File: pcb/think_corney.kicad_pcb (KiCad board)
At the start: 2 copper layers, 130.3 x 86.5 mm, 112 parts

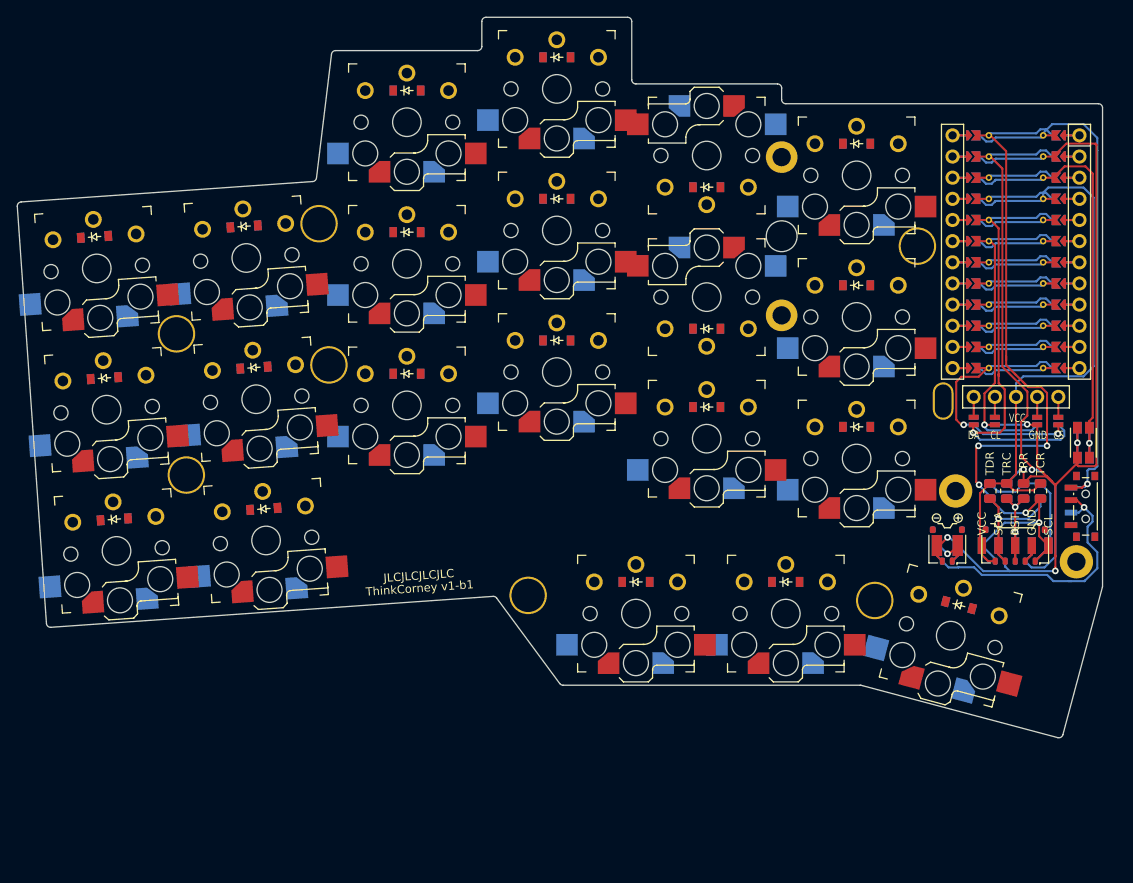
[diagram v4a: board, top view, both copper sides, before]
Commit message: Traces: Added initial matrix traces
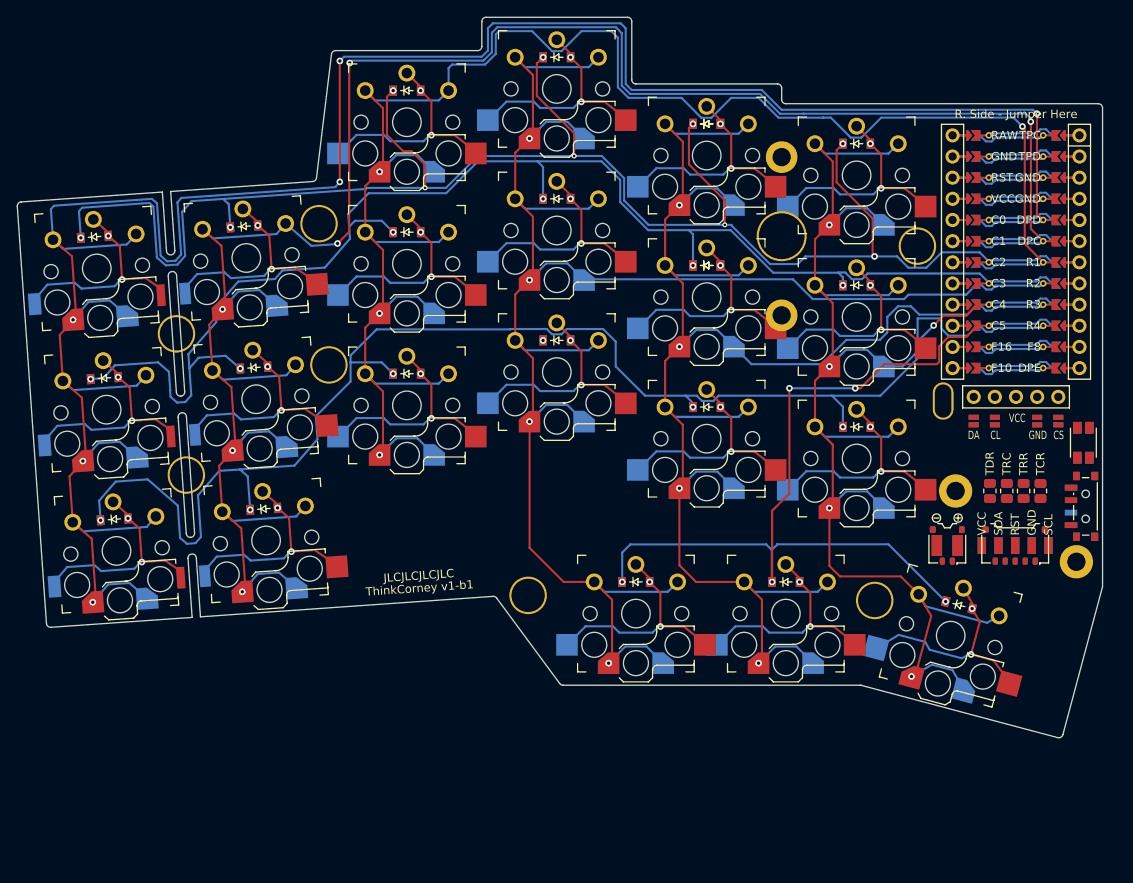
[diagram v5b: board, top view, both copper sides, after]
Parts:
- added D22: , ComboDiode, F.Cu at (170.9, 65.7)
- added D23: , ComboDiode, F.Cu at (170.9, 48.7)
- moved S19 96.0 mm to (115.6, 64.8), turned to -176 degrees
- moved S16 91.9 mm to (97.6, 66.1), turned to -176 degrees
- moved S15 90.7 mm to (98.8, 83.0), turned to -176 degrees
- moved S14 89.6 mm to (100.0, 100.0), turned to -176 degrees
- moved S12 68.7 mm to (180.4, 107.5)
- moved S18 68.6 mm to (116.8, 81.8), turned to -176 degrees
- moved S8 58.8 mm to (188.9, 88.9)
- moved S9 58.8 mm to (188.9, 71.9)
- moved D21 58.6 mm to (201.1, 106.5), turned to -15 degrees
- moved D18 53.3 mm to (188.9, 51.1)
- moved S11 47.0 mm to (162.4, 107.5)
- moved S17 45.3 mm to (118.0, 98.7), turned to -176 degrees
- moved D17 44.4 mm to (188.9, 68.1)
- moved S10 43.1 mm to (188.9, 54.9)
- moved S6 42.5 mm to (152.9, 44.5), turned to 180 degrees
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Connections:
- D14 pad 1: R3 -> R2
- D14 pad 2: inner_bottom -> index_home
- D15 pad 1: R2 -> R1
- D15 pad 2: inner_home -> index_top
- D16 pad 1: R1 -> R3
- D16 pad 2: inner_top -> inner_bottom
- D17 pad 1: R4 -> R2
- D17 pad 2: outer_cluster -> inner_home
- D18 pad 1: R4 -> R1
- D18 pad 2: home_cluster -> inner_top
- D19 pad 2: inner_cluster -> outer_cluster
- D20 pad 1: R2 -> R4
- D20 pad 2: index_home -> home_cluster
- D21 pad 1: R1 -> R4
- D21 pad 2: index_top -> inner_cluster
- MCU1 pad 113: F10 -> DPE
- MCU1 pad 114: F16 -> F8
- MCU1 pad 115: C5 -> R4
- MCU1 pad 116: C4 -> R3
- MCU1 pad 117: C3 -> R2
- MCU1 pad 118: C2 -> R1
- MCU1 pad 119: C1 -> DPC
- MCU1 pad 120: C0 -> DPD
- MCU1 pad 121: VCC -> GND
- MCU1 pad 122: RST -> GND
- MCU1 pad 123: GND -> TPD
- MCU1 pad 124: RAW -> TPC
- S1 pad 1: C0 -> C2
- S1 pad 2: outer_bottom -> ring_bottom
- S10 pad 1: C3 -> C5
- S10 pad 2: middle_bottom -> inner_top
- S11 pad 2: middle_home -> outer_cluster
- S12 pad 1: C3 -> C4
- S12 pad 2: middle_top -> home_cluster
- S13 pad 1: C4 -> C5
- S13 pad 2: index_bottom -> inner_cluster
- S14 pad 1: C5 -> C0
- S14 pad 2: inner_bottom -> outer_bottom
- S15 pad 1: C5 -> C0
- S15 pad 2: inner_home -> outer_home
- S16 pad 1: C5 -> C0
- S16 pad 2: inner_top -> outer_top
- S17 pad 1: C3 -> C1
- S17 pad 2: outer_cluster -> pinky_bottom
- S18 pad 1: C4 -> C1
- S18 pad 2: home_cluster -> pinky_home
- S19 pad 1: C5 -> C1
- S19 pad 2: inner_cluster -> pinky_top
- S2 pad 1: C0 -> C2
- S2 pad 2: outer_home -> ring_home
- S3 pad 1: C0 -> C2
- S3 pad 2: outer_top -> ring_top
- S4 pad 1: C1 -> C3
- S4 pad 2: pinky_bottom -> middle_bottom
- S5 pad 1: C1 -> C3
- S5 pad 2: pinky_home -> middle_home
- S6 pad 1: C1 -> C3
- S6 pad 2: pinky_top -> middle_top
- S7 pad 1: C2 -> C4
- S7 pad 2: ring_bottom -> index_bottom
- S8 pad 1: C2 -> C5
- S8 pad 2: ring_home -> inner_bottom
- S9 pad 1: C2 -> C5
- S9 pad 2: ring_top -> inner_home
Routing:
- net C0: track 10.1 -> 291.7 mm, vias 0 -> 6
- net C1: track 10.1 -> 254.1 mm, vias 0 -> 6
- net C2: track 10.1 -> 222.4 mm, vias 0 -> 4
- net C3: track 10.1 -> 219.3 mm, vias 0 -> 4
- net R1: track 10.2 -> 208.7 mm, vias 0 -> 10
- net C4: track 10.1 -> 206.3 mm, vias 0 -> 4
- net C5: track 10.1 -> 182.8 mm, vias 0 -> 4
- net R2: track 10.2 -> 173.4 mm, vias 0 -> 6
- net R3: track 10.2 -> 169.9 mm, vias 0 -> 7
- net GND: track 149.3 -> 30.5 mm, vias 5 -> 0
- net R4: track 10.2 -> 110.9 mm, vias 0 -> 5
- net VCC: track 96.3 -> 10.1 mm
- net F16: track 94.5 -> 10.1 mm, vias 5 -> 0
- net TPD: track 84.4 -> 10.2 mm, vias 2 -> 0
- net RAW: track 65.0 -> 10.1 mm, vias 1 -> 0
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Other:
- outline, holes or cut-outs redrawn

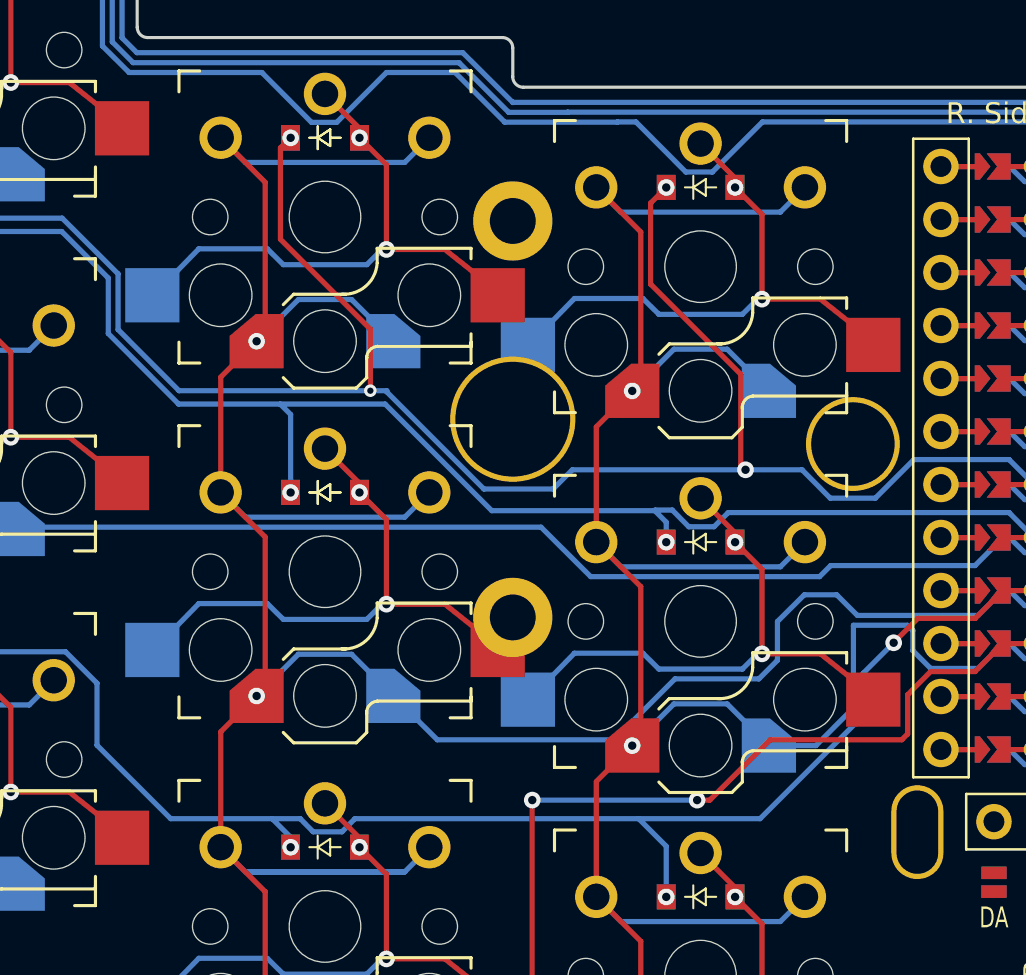
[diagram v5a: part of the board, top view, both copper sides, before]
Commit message: Traces: Fixed matrix traces for TP key changes
Added pcb
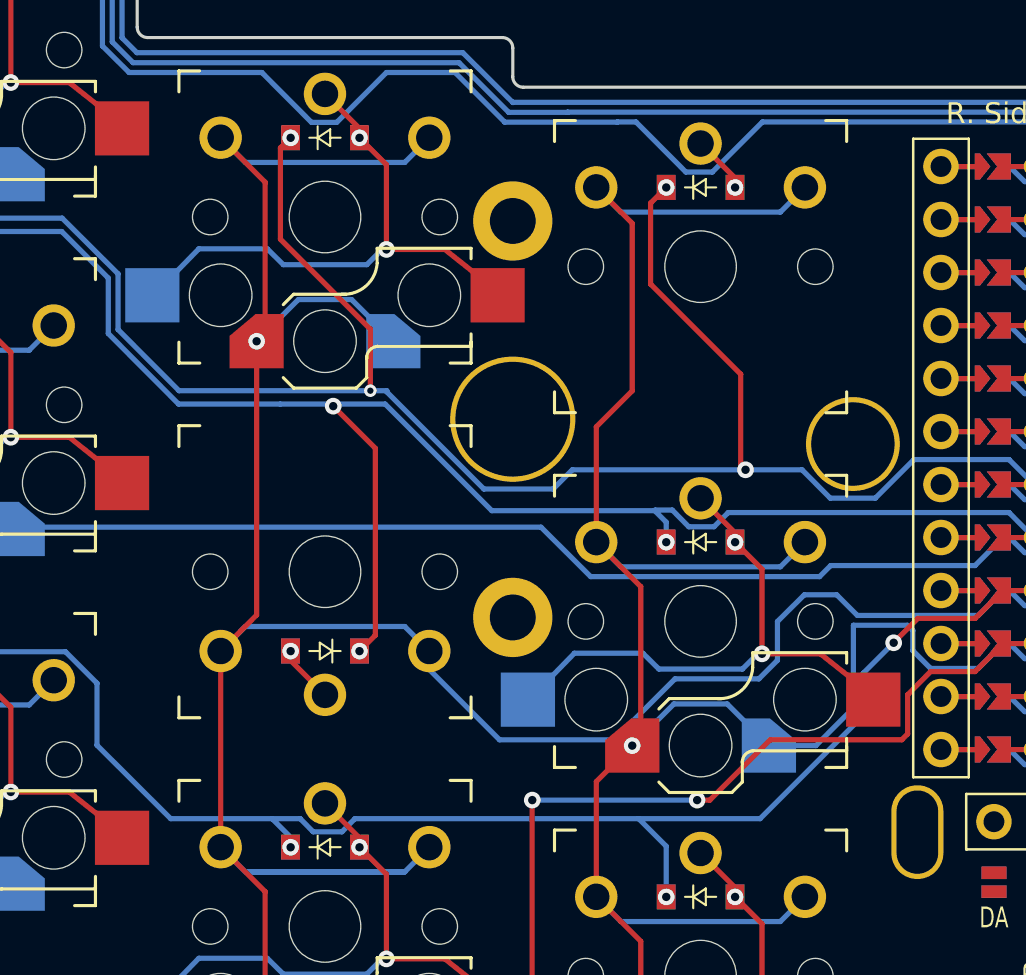
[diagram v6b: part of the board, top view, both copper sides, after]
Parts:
- removed D22, D23: , ComboDiode
- moved S13 104.9 mm to (98.8, 83.0), turned to -176 degrees
- moved S12 80.7 mm to (100.0, 100.0), turned to -176 degrees
- moved S18 61.5 mm to (170.9, 52.5), turned to 180 degrees
- moved D15 55.7 mm to (162.4, 103.7)
- moved S19 55.5 mm to (170.9, 69.5), turned to 180 degrees
- moved D20 53.3 mm to (188.9, 51.1)
- moved S10 53.3 mm to (180.4, 107.5)
- moved S9 44.4 mm to (162.4, 107.5)
- moved D17 40.3 mm to (201.1, 106.5), turned to -15 degrees
- moved D21 40.3 mm to (188.9, 68.1), turned to 0 degrees
- moved S11 37.9 mm to (200.2, 110.2), turned to 165 degrees
- moved S14 34.0 mm to (97.6, 66.1)
- moved S17 34.0 mm to (115.6, 64.8)
- moved D19 31.6 mm to (170.9, 73.3), turned to 180 degrees
- moved D14 26.4 mm to (188.9, 85.1)
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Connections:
- D14 pad 1: R2 -> R3
- D14 pad 2: index_home -> inner_bottom
- D15 pad 1: R1 -> R4
- D15 pad 2: index_top -> outer_cluster
- D16 pad 1: R3 -> R4
- D16 pad 2: inner_bottom -> home_cluster
- D17 pad 1: R2 -> R4
- D17 pad 2: inner_home -> inner_cluster
- D18 pad 2: inner_top -> index_top
- D19 pad 1: R4 -> R2
- D19 pad 2: outer_cluster -> index_home
- D20 pad 1: R4 -> R1
- D20 pad 2: home_cluster -> inner_top
- D21 pad 1: R4 -> R2
- D21 pad 2: inner_cluster -> inner_home
- S10 pad 1: C5 -> C4
- S10 pad 2: inner_top -> home_cluster
- S11 pad 1: C3 -> C5
- S11 pad 2: outer_cluster -> inner_cluster
- S12 pad 1: C4 -> C0
- S12 pad 2: home_cluster -> outer_bottom
- S13 pad 1: C5 -> C0
- S13 pad 2: inner_cluster -> outer_home
- S14 pad 2: outer_bottom -> outer_top
- S15 pad 1: C0 -> C1
- S15 pad 2: outer_home -> pinky_bottom
- S16 pad 1: C0 -> C1
- S16 pad 2: outer_top -> pinky_home
- S17 pad 2: pinky_bottom -> pinky_top
- S18 pad 1: C1 -> C4
- S18 pad 2: pinky_home -> index_top
- S19 pad 1: C1 -> C4
- S19 pad 2: pinky_top -> index_home
- S20 pad 1: C4 -> C5
- S20 pad 2: index_home -> inner_top
- S21 pad 1: C4 -> C5
- S21 pad 2: index_top -> inner_home
- S9 pad 1: C5 -> C3
- S9 pad 2: inner_home -> outer_cluster
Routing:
- net index_home: track 24.7 -> 2.78 mm, vias 2 -> 1
- net inner_top: track 24.7 -> 2.78 mm, vias 2 -> 1
- net C4: track 206.3 -> 196.0 mm, vias 4 -> 3
- net C5: track 182.8 -> 174.2 mm, vias 4 -> 3
- net R2: track 173.4 -> 181.9 mm, vias 6 -> 7

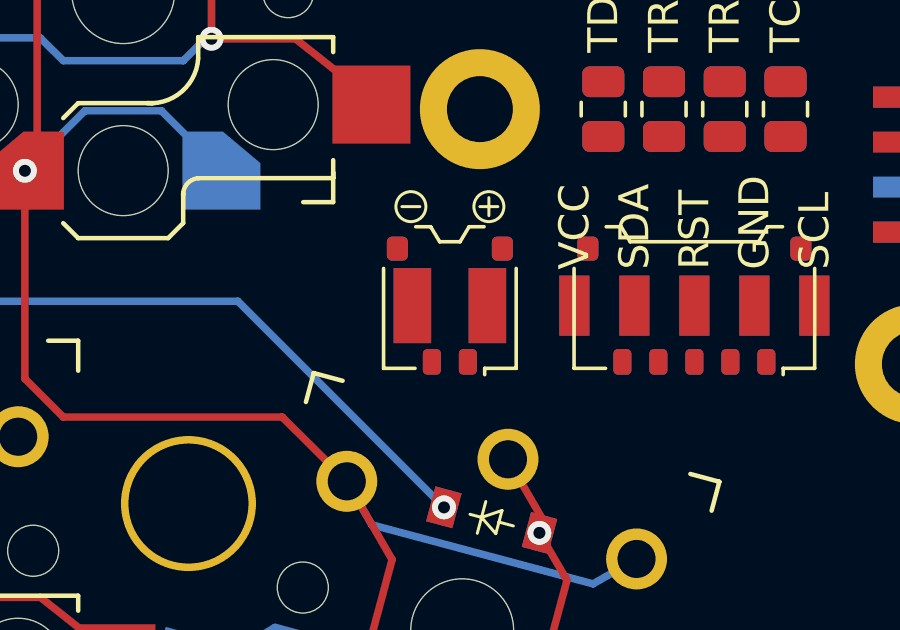
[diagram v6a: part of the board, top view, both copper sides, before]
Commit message: Traces: Added traces for batter conn + pad
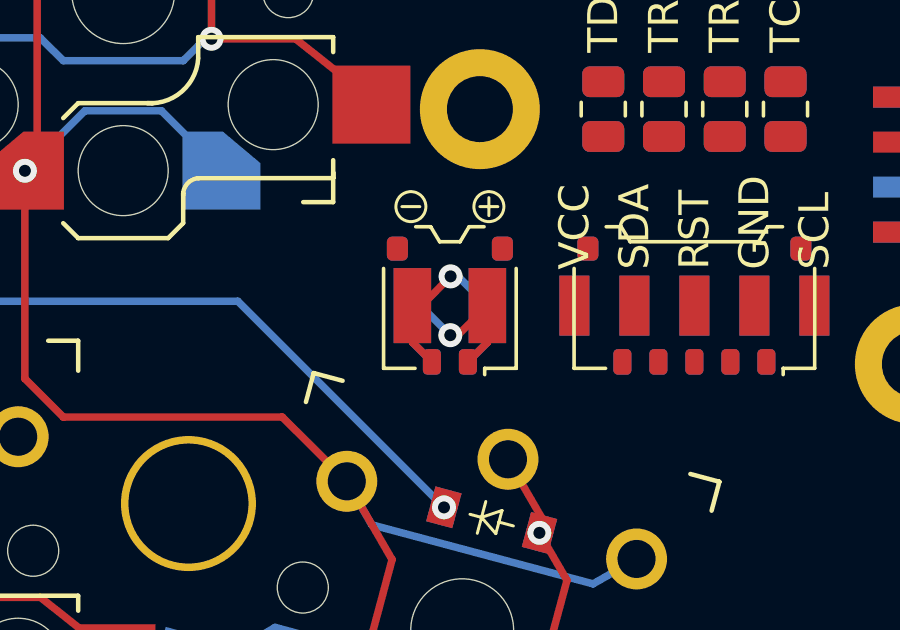
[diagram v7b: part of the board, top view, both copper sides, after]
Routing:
- net GND: track 30.5 -> 38.1 mm, vias 0 -> 1
- net BAT_P: track 0.00 -> 7.58 mm, vias 0 -> 1

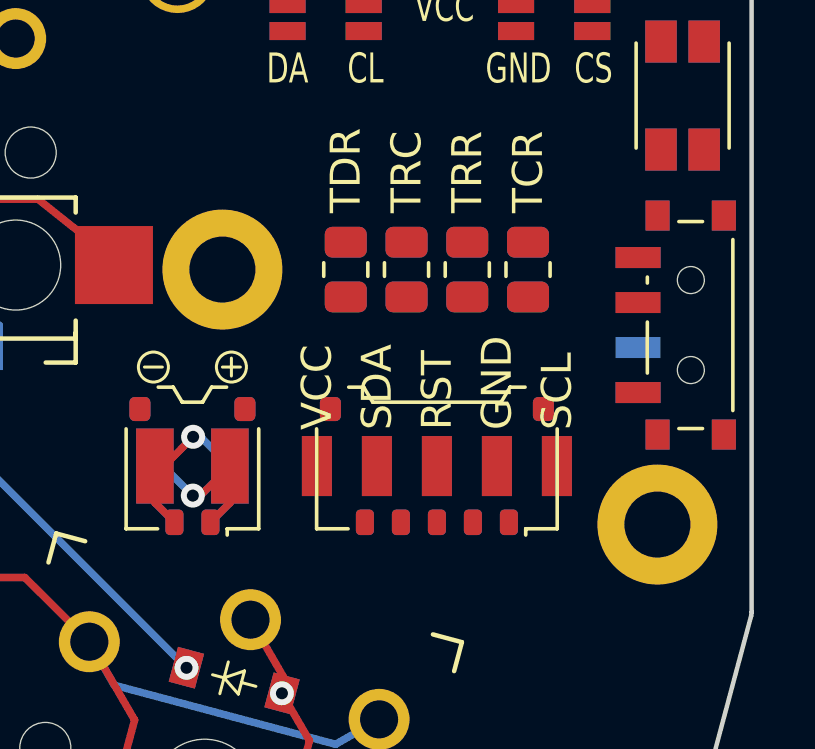
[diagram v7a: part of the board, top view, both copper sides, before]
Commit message: Traces: Added trackpoint conn traces
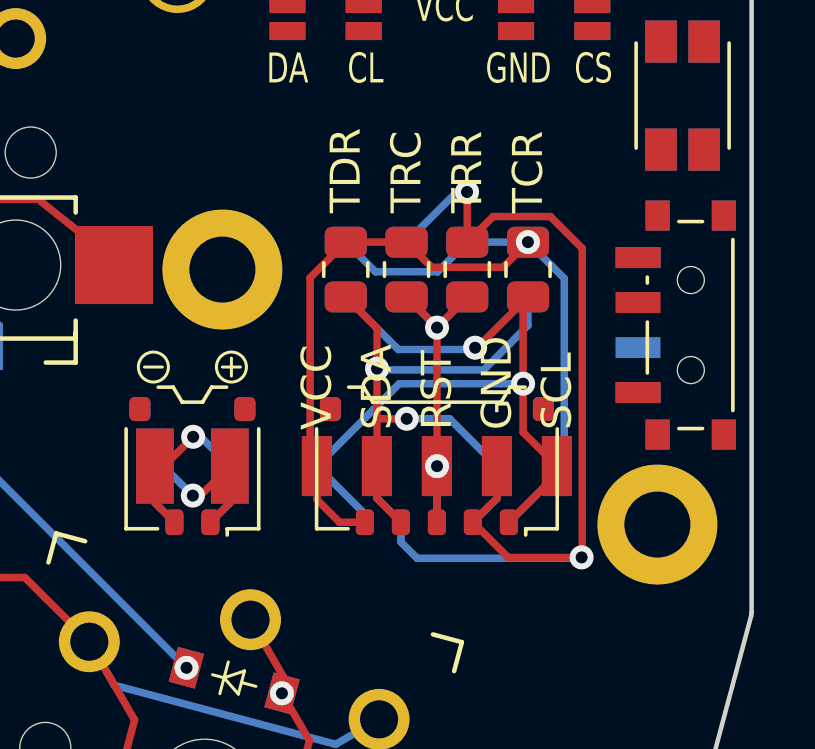
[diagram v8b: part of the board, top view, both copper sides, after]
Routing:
- net VCC: track 10.1 -> 45.2 mm, vias 0 -> 1
- net GND: track 38.1 -> 72.7 mm, vias 1 -> 3
- net TPC: track 10.2 -> 36.2 mm, vias 0 -> 2
- net TPD: track 10.2 -> 31.9 mm, vias 0 -> 2
- net TPR: track 0.00 -> 14.1 mm, vias 0 -> 2
